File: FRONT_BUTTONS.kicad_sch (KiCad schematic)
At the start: 20 parts, among them J5 Micro_SD_Card_CD, J6 Conn_01x18_Socket, Q2 BC817, SW10 SW_Push, SW11 SW_Push, SW12 SW_Push, SW2 SW_Push, SW3 SW_Push, SW4 SW_Push, SW5 SW_Push, SW9 SW_Push

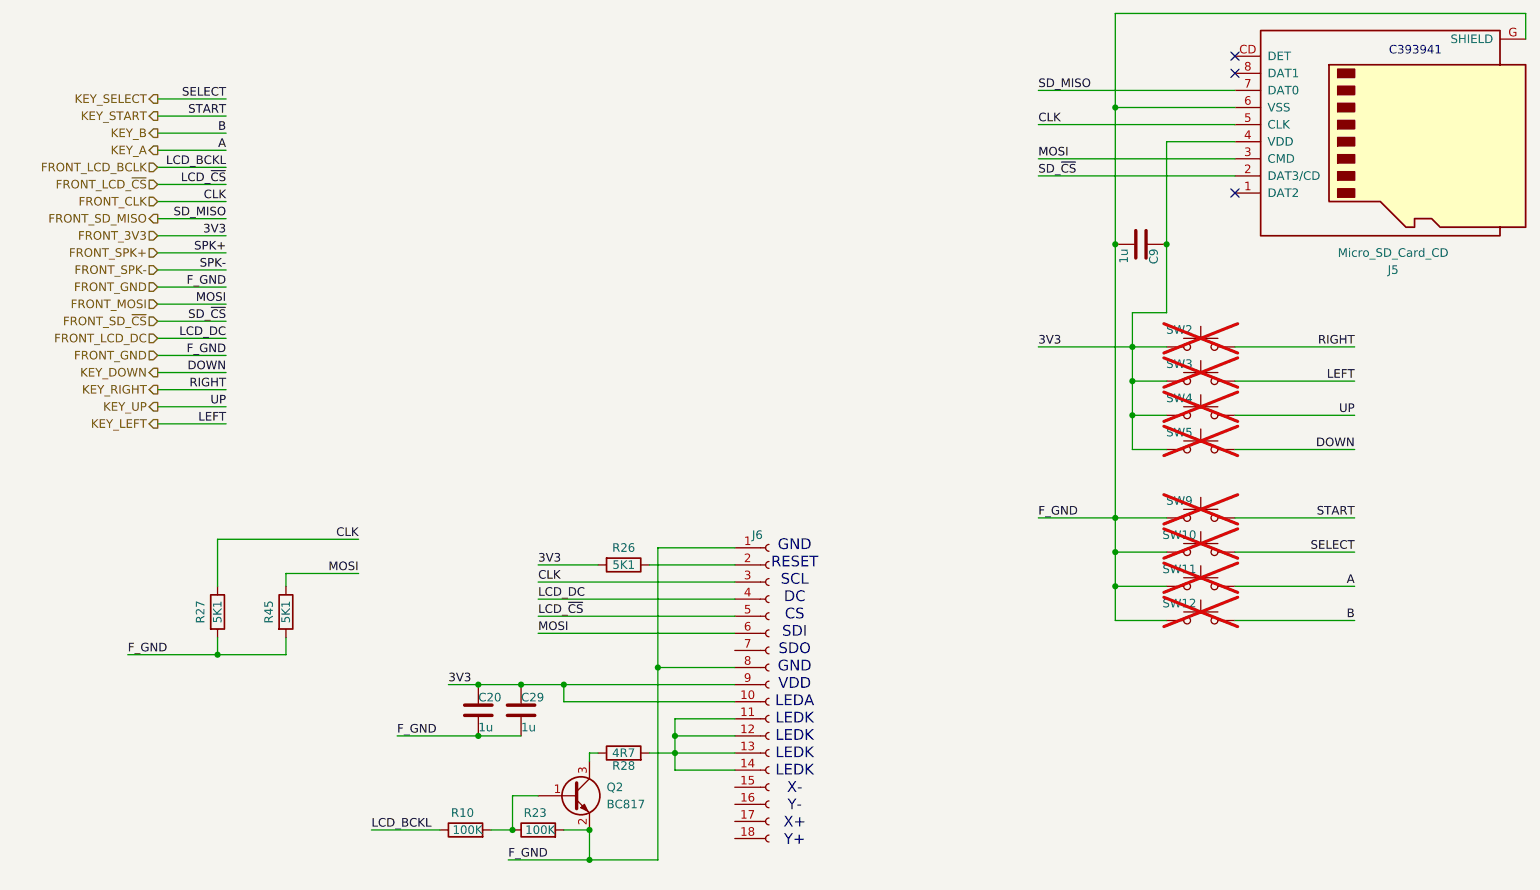
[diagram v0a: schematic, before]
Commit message: update online version before change to esp32 s3
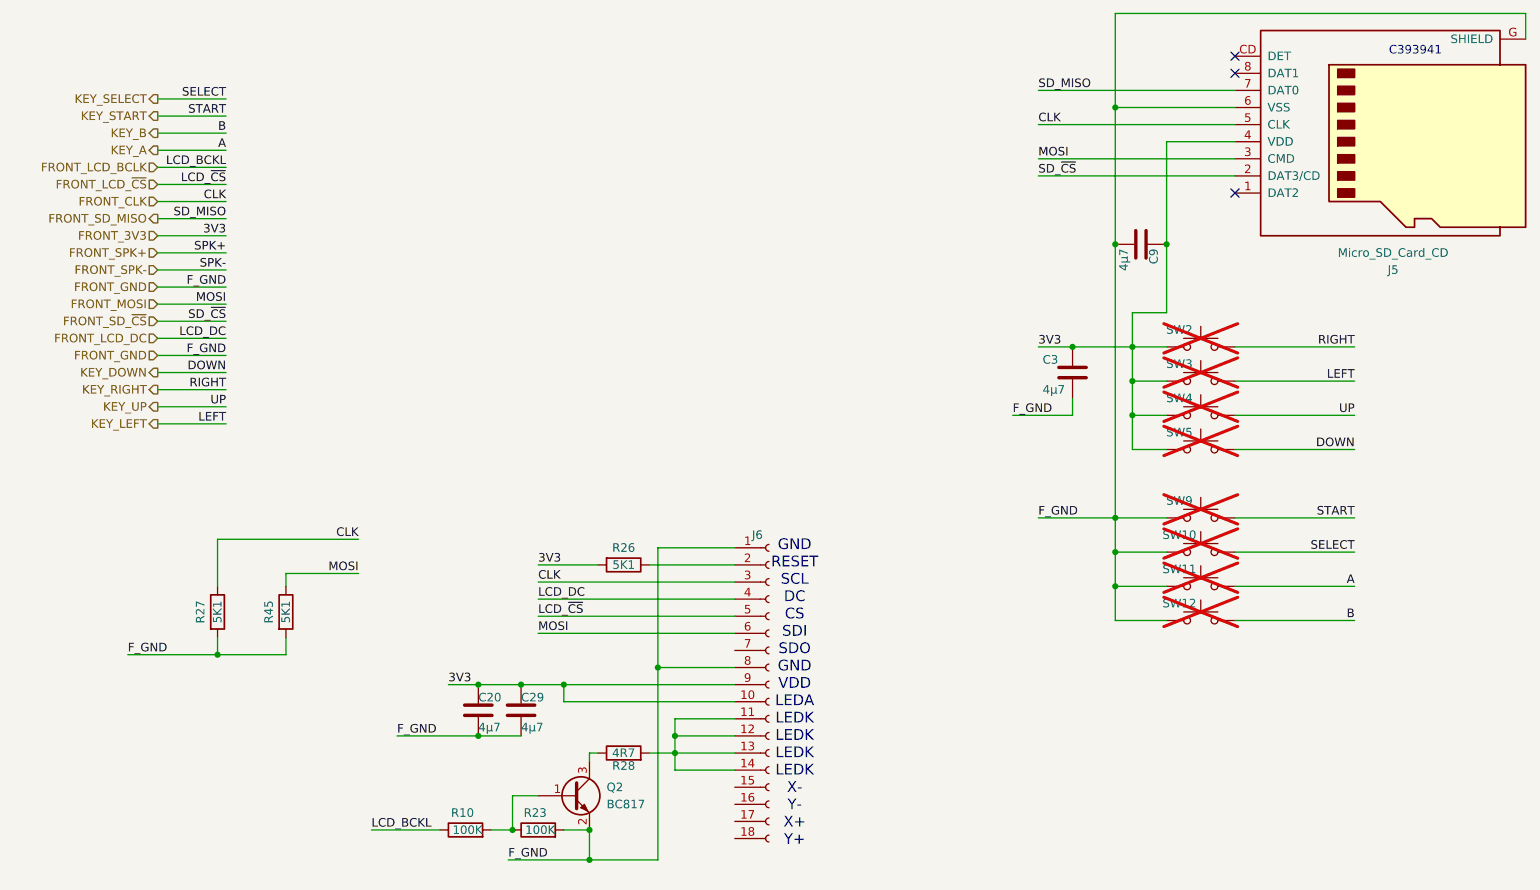
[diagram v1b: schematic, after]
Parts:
- added C3: 4µ7, Capacitor_SMD:C_0603_1608Metric, symbol Device:C
- C20, C29, C9: value 1u -> 4µ7; LCSC C5673 -> C69335
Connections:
- net FRONT_3V3: now also C3.1
- net FRONT_GND: now also C3.2
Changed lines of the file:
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@@
 	)
 	(junction
+		(at 175.26 93.98)
+		(diameter 0)
+		(color 0 0 0 0)
+	)
+	(junction
 		(at 113.665 141.605)
 		(diameter 0)
@@
 	(wire
 		(pts
-			(xy 170.18 93.98) (xy 184.15 93.98)
+			(xy 170.18 93.98) (xy 175.26 93.98)
 		)
 		(stroke
@@
 	(wire
 		(pts
+			(xy 175.26 104.14) (xy 166.37 104.14)
+		)
+		(stroke
+			(width 0)
+			(type default)
+		)
+	)
+	(wire
+		(pts
 			(xy 49.53 95.25) (xy 39.37 95.25)
 		)
@@
 	(wire
 		(pts
+			(xy 175.26 101.6) (xy 175.26 104.14)
+		)
+		(stroke
+			(width 0)
+			(type default)
+		)
+	)
+	(wire
+		(pts
+			(xy 175.26 93.98) (xy 184.15 93.98)
+		)
+		(stroke
+			(width 0)
+			(type default)
+		)
+	)
+	(wire
+		(pts
 			(xy 181.61 119.38) (xy 181.61 124.46)
 		)
@@
 	)
 	(label "F_GND"
+		(at 166.37 104.14 0)
+		(fields_autoplaced yes)
+		(effects
+			(font
+				(size 1.27 1.27)
+			)
+			(justify left bottom)
+		)
+	)
+	(label "F_GND"
 		(at 34.925 139.7 0)
 		(fields_autoplaced yes)
@@
 	)
 	(symbol
+		(lib_id "Device:C")
+		(at 175.26 97.79 0)
+		(unit 1)
+		(exclude_from_sim no)
+		(in_bom yes)
+		(on_board yes)
+		(dnp no)
+		(property "Reference" "C3"
+			(at 170.815 95.885 0)
+			(effects
+				(font
+					(size 1.27 1.27)
+				)
+				(justify left)
+			)
+		)
+		(property "Value" "4µ7"
+			(at 170.815 100.33 0)
+			(effects
+				(font
+					(size 1.27 1.27)
+				)
+				(justify left)
+			)
+		)
+		(property "Footprint" "Capacitor_SMD:C_0603_1608Metric"
+			(at 176.2252 101.6 0)
+			(effects
+				(font
+					(size 1.27 1.27)
+				)
+				(hide yes)
+			)
+		)
+		(property "Datasheet" "~"
+			(at 175.26 97.79 0)
+			(effects
+				(font
+					(size 1.27 1.27)
+				)
+				(hide yes)
+			)
+		)
+		(property "Description" "25V"
+			(at 175.26 97.79 0)
+			(effects
+				(font
+					(size 1.27 1.27)
+				)
+				(hide yes)
+			)
+		)
+		(property "LCSC" "C69335"
+			(at 175.26 97.79 0)
+			(effects
+				(font
+					(size 1.27 1.27)
+				)
+				(hide yes)
+			)
+		)
+		(property "SOURCED" "ok"
+			(at 175.26 97.79 0)
+			(effects
+				(font
+					(size 1.27 1.27)
+				)
+				(hide yes)
+			)
+		)
+		(pin "1"
+		)
+		(pin "2"
+		)
+		(instances
+			(project "ILI9341_ESP32_GBC"
+				(path "/ff5a7903-456b-49e1-a9c0-cc21ca8443ce/d975582f-4378-40f0-9d4d-51d3304967f8"
+					(reference "C3")
+					(unit 1)
+				)
+			)
+		)
+	)
+	(symbol
 		(lib_id "Device:R")
 		(at 58.42 133.35 0)
@@
 			)
 		)
-		(property "Value" "1u"
+		(property "Value" "4µ7"
 			(at 182.88 79.375 0)
 			(effects
@@
 			)
 		)
-		(property "LCSC" "C5673"
+		(property "LCSC" "C69335"
 			(at 185.42 78.74 0)
 			(effects
@@
 			)
 		)
-		(property "Value" "1u"
+		(property "Value" "4µ7"
 			(at 86.995 150.495 0)
 			(effects
@@
 			)
 		)
-		(property "LCSC" "C5673"
+		(property "LCSC" "C69335"
 			(at 86.995 147.955 0)
 			(effects
@@
 			)
 		)
-		(property "Value" "1u"
+		(property "Value" "4µ7"
 			(at 93.345 150.495 0)
 			(effects
@@
 			)
 		)
-		(property "LCSC" "C5673"
+		(property "LCSC" "C69335"
 			(at 93.345 147.955 0)
 			(effects

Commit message: updated version with esp32 s3 and i2s audio ic
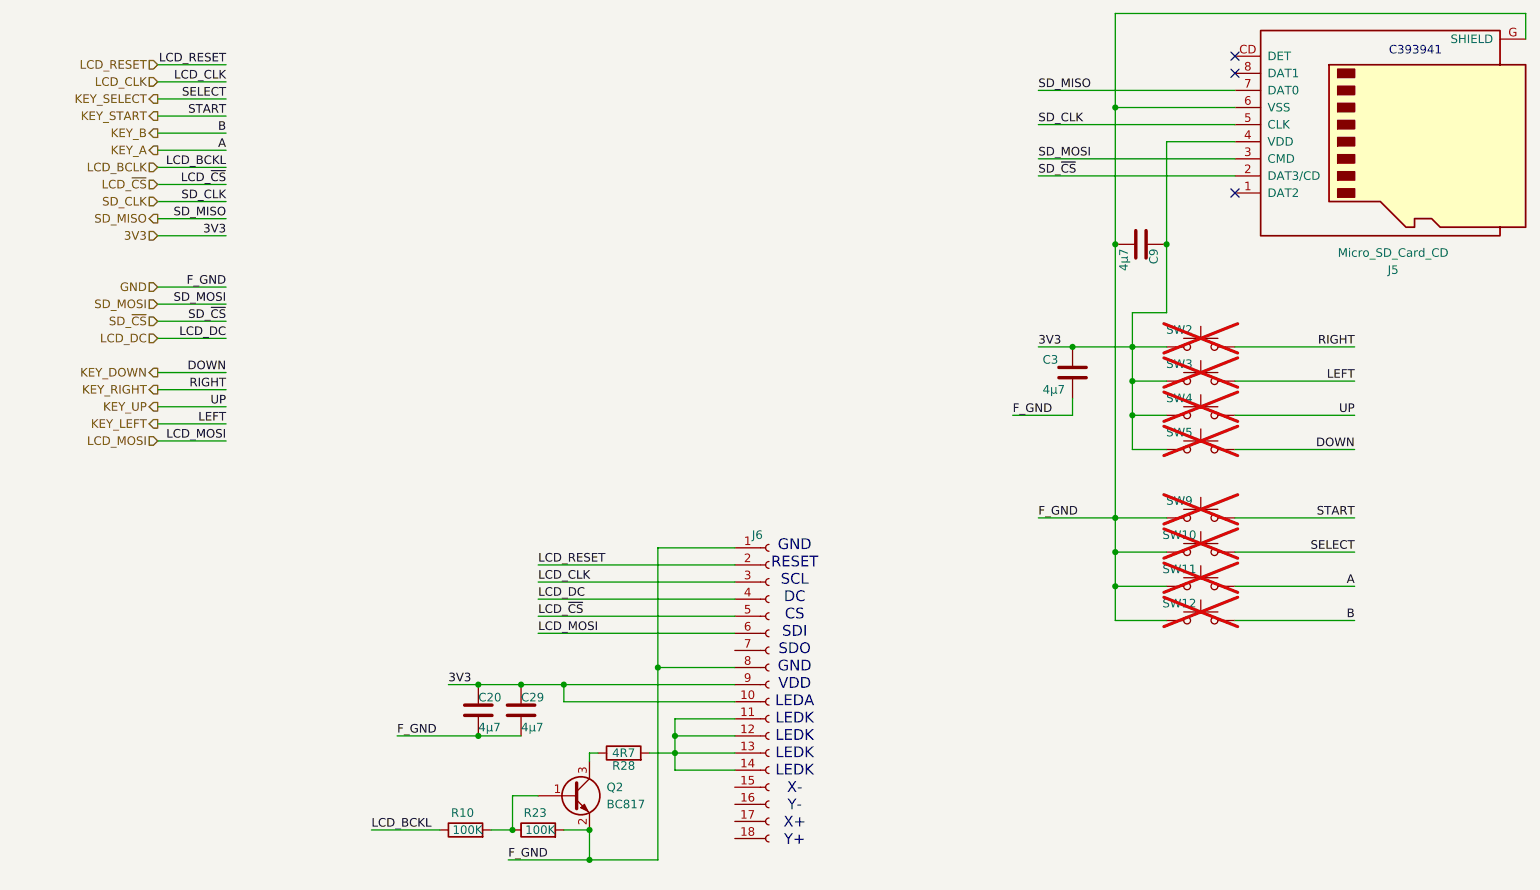
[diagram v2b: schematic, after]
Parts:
- removed R26, R27, R45: 5K1, Resistor_SMD:R_0603_1608Metric, symbol Device:R
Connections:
- net LCD_RESET: now reaches J6.2 (Pin_2)
- net FRONT_3V3 renamed 3V3
- net FRONT_CLK renamed LCD_CLK
- net LCD_CLK: no longer J5.5 (CLK)
- net FRONT_GND renamed GND
- net FRONT_LCD_BCLK renamed LCD_BCLK
- net FRONT_LCD_DC renamed LCD_DC
- net FRONT_LCD_~{CS} renamed LCD_~{CS}
- net FRONT_MOSI renamed LCD_MOSI
- net LCD_MOSI: no longer J5.3 (CMD)
- net FRONT_SD_MISO renamed SD_MISO
- net FRONT_SD_~{CS} renamed SD_~{CS}
- new net SD_CLK: J5.5 (CLK)
- new net SD_MOSI: J5.3 (CMD)

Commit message: Order V1
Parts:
- added CN1: KH-CL0.5-H2.0-18PS, easyeda2kicad:FPC-SMD_KH-CL0.5-H2.0-18PS, symbol easyeda2kicad:KH-CL0.5-H2.0-18PS
- added FPC1: 0.8K-BS-18PWB(H=2.0), easyeda2kicad:FPC-SMD_18P-P0.80_HDGC_0.8K-BS-18PWB, symbol easyeda2kicad:0.8K-BS-18PWB(H=2.0)
- J6: ALI (none) -> https://de.aliexpress.com/item/32861524235.html
- SW2, SW3, SW4, SW5: footprint TheBrutzlers_Lib:RubberpadButton_250µ_250µ -> TheBrutzlers_Lib:RubberpadButton_GBC_CROSS
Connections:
- net 3V3: now also SW5.2, CN1.10, CN1.9, FPC1.10, FPC1.9; no longer SW5.1
- net GND: now also CN1.1, CN1.19, CN1.20, CN1.8, FPC1.11, FPC1.18, FPC1.19, FPC1.20
- net KEY_DOWN: now also SW5.1; no longer SW5.2
- net LCD_CLK: now also CN1.3, FPC1.16
- net LCD_DC: now also CN1.4, FPC1.15
- net LCD_MOSI: now also CN1.6, FPC1.13
- net LCD_RESET: now also CN1.2, FPC1.17
- net LCD_~{CS}: now also CN1.5, FPC1.14
- net at J6.11 (Pin_11), J6.12 (Pin_12), J6.13 (Pin_13)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: now also CN1.11, CN1.12, CN1.13, CN1.14, FPC1.5, FPC1.6, FPC1.7, FPC1.8
- net at J6.15 (Pin_15): now also FPC1.4
- net at J6.16 (Pin_16): now also FPC1.3
- net at J6.17 (Pin_17): now also FPC1.2
- net at J6.18 (Pin_18): now also FPC1.1
- net at J6.7 (Pin_7): now also FPC1.12
